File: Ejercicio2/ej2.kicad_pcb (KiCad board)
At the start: 2 copper layers, 40.6 x 61 mm, 13 parts, among them J1 DB9-F, J2 CAN, U1 SP3232ECN, U2 AMIS42665TJAA1RG

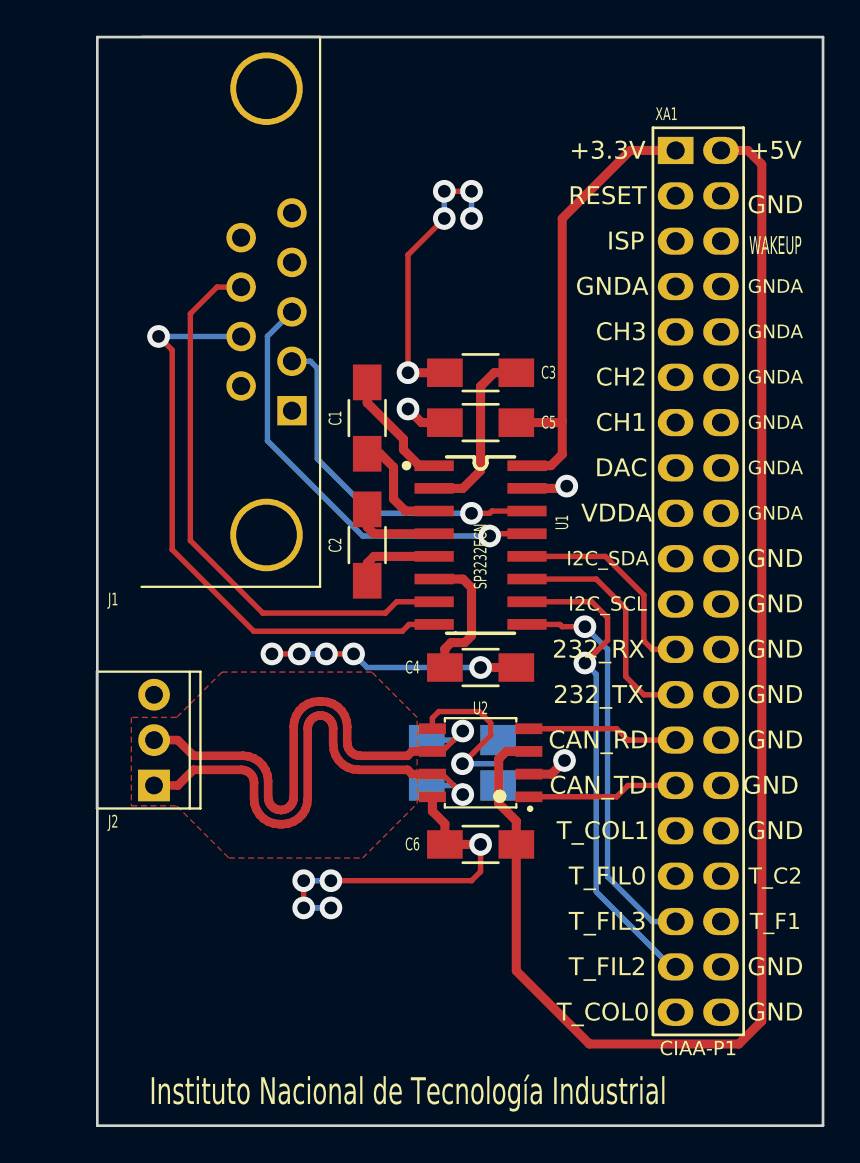
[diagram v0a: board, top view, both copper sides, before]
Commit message: Agregado logos y plantillas al ejercicio 2.
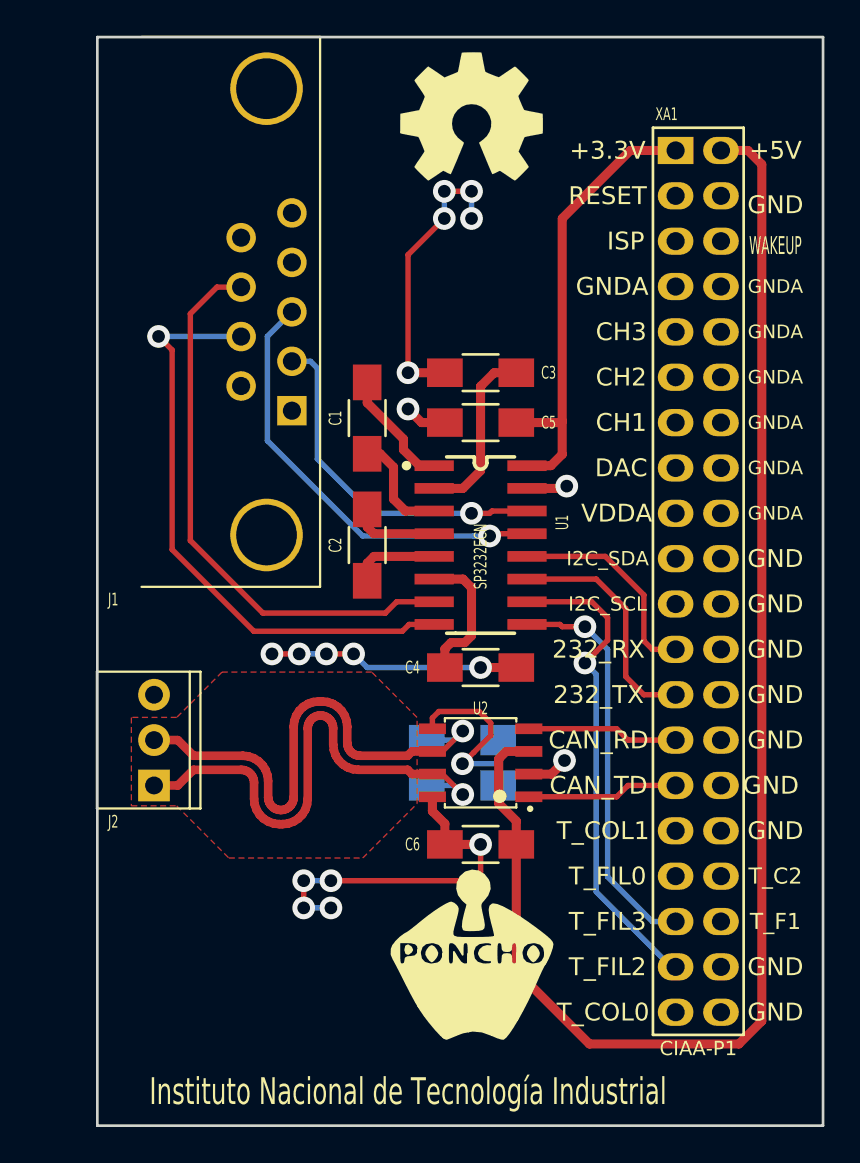
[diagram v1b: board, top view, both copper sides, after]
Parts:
- added G***: LOGO, ej2:Logo_Poncho, F.Cu at (123.2, 125.1)
- added G101: Logo_OSHWA, ej2:Logo_OSHWA, F.Cu at (123.2, 78.1)

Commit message: Completo rótulo y agrego leyendas al PCB.
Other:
- board text added: "En un circuito multicapa anotar la información del stack-up dentro del diseño"
- board text added: "Falta realizar agujeros o recorte para ver los LEDs de la EDU-CIAA"
- board text added: "L1 L2"
- board text added: "No olvidar el rótulo también en el PCB."
- board text added: "Stack-Up"
- board text added: "Terminación superficial: HASL Espesor final aprox.: 1,6 mm"
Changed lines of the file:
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@@
     (links 44)
     (no_connects 0)
-    (area 102.159999 73.584999 142.950001 134.695001)
+    (area 81.072618 65.73 157.923572 134.695001)
     (thickness 1.6)
-    (drawings 9)
+    (drawings 23)
     (tracks 289)
     (zones 0)
@@
   (page A4)
   (title_block
-    (title "Ejercicio 2 - Curso Kicad")
-    (date 2015-11-20)
+    (title "Ejercicio 2 - Curso Kicad - Poncho RS232 y CAN")
+    (date 2015-11-26)
     (rev 1.0)
     (company "Instituto Nacional de Tecnología Industrial")
+    (comment 1 "Autores: D.Brengi, D. Alamon y N. Scotti")
   )
   (layers
@@
       (xy 3.778435 -0.1467) (xy 3.778435 -0.1467)) (layer F.SilkS) (width 0.1))
   )
+  (gr_text "No olvidar el rótulo\ntambién en el PCB." (at 221.615 146.05) (layer Dwgs.User)
+    (effects (font (size 2 2) (thickness 0.2)))
+  )
+  (gr_line (start 222.885 164.465) (end 222.885 150.495) (angle 90) (layer Dwgs.User) (width 0.127))
+  (gr_line (start 222.885 164.465) (end 224.79 162.56) (angle 90) (layer Dwgs.User) (width 0.127))
+  (gr_line (start 222.885 164.465) (end 220.98 162.56) (angle 90) (layer Dwgs.User) (width 0.127))
+  (gr_text "En un circuito multicapa \nanotar la información del\nstack-up dentro del diseño" (at 170.815 67.31) (layer Dwgs.User)
+    (effects (font (size 2 2) (thickness 0.3) italic) (justify left))
+  )
+  (gr_text "L1\n\nL2" (at 203.2 87.63) (layer Dwgs.User)
+    (effects (font (size 2 2) (thickness 0.3)))
+  )
+  (gr_line (start 174.625 90.805) (end 198.755 90.805) (angle 90) (layer Dwgs.User) (width 0.3))
+  (gr_line (start 174.625 85.09) (end 198.755 85.09) (angle 90) (layer Dwgs.User) (width 0.3))
+  (gr_text "Terminación superficial: HASL\nEspesor final aprox.: 1,6 mm" (at 191.77 100.965) (layer Dwgs.User)
+    (effects (font (size 2 2) (thickness 0.3)))
+  )
+  (gr_text Stack-Up (at 188.595 75.565) (layer Dwgs.User)
+    (effects (font (size 3 3) (thickness 0.5)))
+  )
+  (gr_text "Falta realizar agujeros\no recorte para ver\nlos LEDs de la EDU-CIAA" (at 88.9 127.635) (layer Dwgs.User)
+    (effects (font (size 0.78 0.8) (thickness 0.15)))
+  )
+  (gr_line (start 97.79 133.985) (end 100.965 133.985) (angle 90) (layer Dwgs.User) (width 0.127))
+  (gr_line (start 97.79 123.825) (end 97.79 133.985) (angle 90) (layer Dwgs.User) (width 0.127))
+  (gr_line (start 100.965 123.825) (end 97.79 123.825) (angle 90) (layer Dwgs.User) (width 0.127))
   (dimension 40.64 (width 0.3) (layer Dwgs.User)
     (gr_text 40,640mm (at 122.555 67.23) (layer Dwgs.User)
